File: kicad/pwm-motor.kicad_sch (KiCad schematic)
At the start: 6 parts, among them M1 Motor_DC, Q3 Q_NMOS

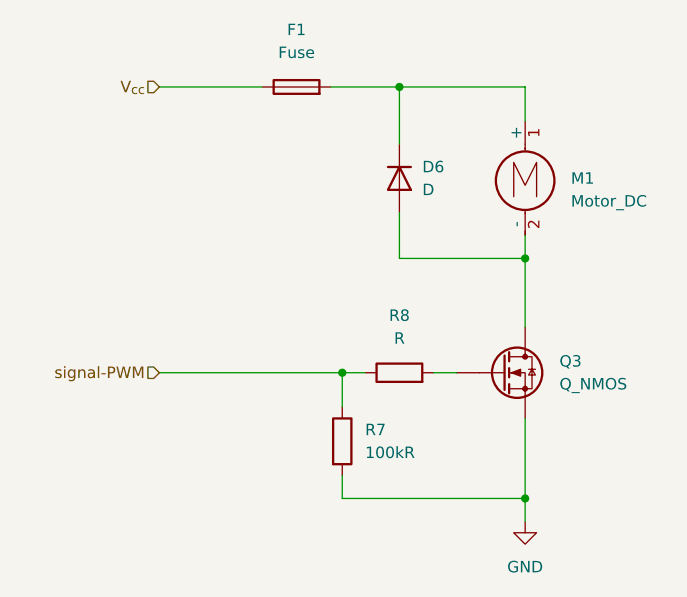
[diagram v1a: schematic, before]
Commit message: terminato collegamento ATMEGA328P
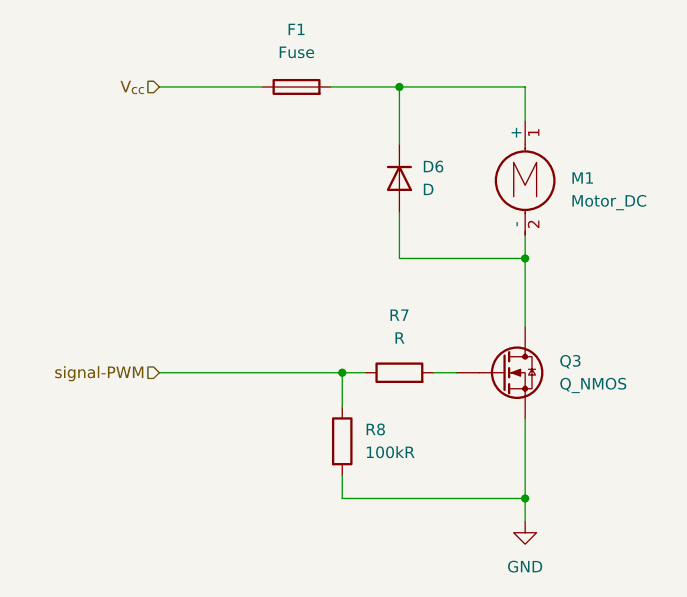
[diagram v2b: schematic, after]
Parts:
- renumbered R8 to R7, R7 to R8
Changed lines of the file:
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@@
 		(dnp no)
 		(fields_autoplaced yes)
-		(property "Reference" "R7"
+		(property "Reference" "R8"
 			(at 52.07 76.1999 0)
 			(effects
@@
 			(project ""
 				(path "/f1ade40e-ee4b-4e00-b57d-44850604005b/90670ac8-15ce-4756-b36a-2162bfc01c8a"
-					(reference "R7")
+					(reference "R8")
 					(unit 1)
 				)
@@
 		(dnp no)
 		(fields_autoplaced yes)
-		(property "Reference" "#PWR024"
+		(property "Reference" "#PWR026"
 			(at 69.85 92.71 0)
 			(effects
@@
 			(project ""
 				(path "/f1ade40e-ee4b-4e00-b57d-44850604005b/90670ac8-15ce-4756-b36a-2162bfc01c8a"
-					(reference "#PWR024")
+					(reference "#PWR026")
 					(unit 1)
 				)
@@
 		(dnp no)
 		(fields_autoplaced yes)
-		(property "Reference" "R8"
+		(property "Reference" "R7"
 			(at 55.88 63.5 90)
 			(effects
@@
 			(project "electronics-schemas"
 				(path "/f1ade40e-ee4b-4e00-b57d-44850604005b/90670ac8-15ce-4756-b36a-2162bfc01c8a"
-					(reference "R8")
-					(unit 1)
-				)
+					(reference "R7")
+					(unit 1)
+				)
